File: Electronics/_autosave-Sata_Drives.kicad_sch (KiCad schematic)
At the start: 66 parts, among them J20 47018-2000, J21 47018-2000, Q2 NPN, Q3 PMOS, Q4 NPN, Q5 PMOS, Q6 PMOS, Q7 NPN, Q8 NPN, Q9 PMOS, U10 JMS561, U9 W25X40CLSN, Y1 30MHz

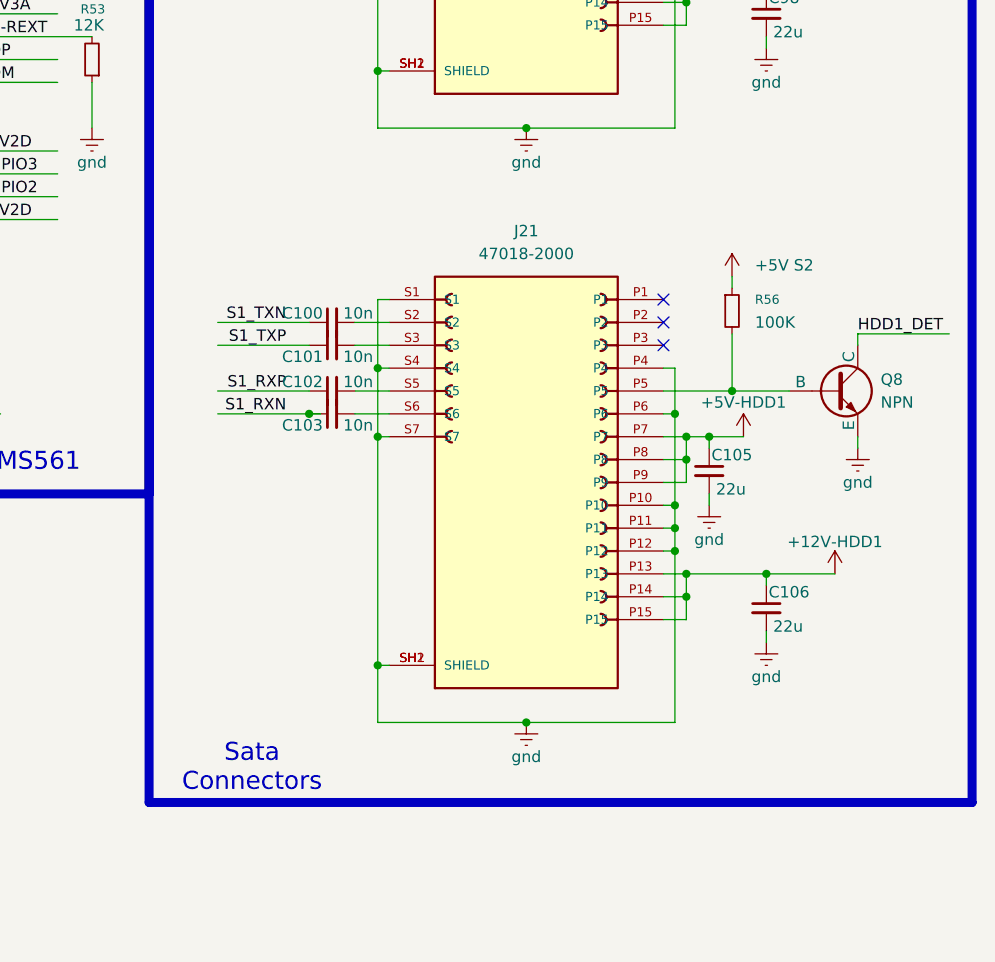
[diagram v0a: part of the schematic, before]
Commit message: Sata Port Changed
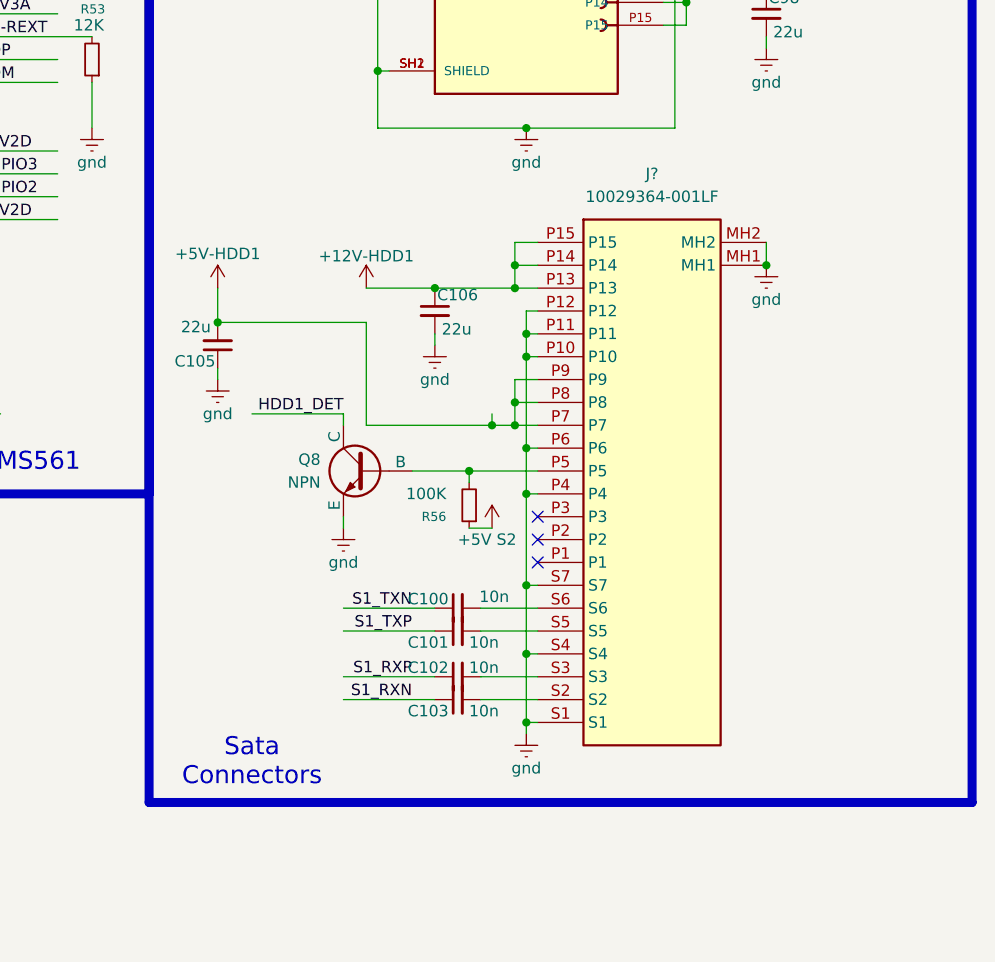
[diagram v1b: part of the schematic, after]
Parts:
- removed J21: 47018-2000, 47018-2000:MOLEX_47018-2000, symbol 47018-2000:47018-2000
- added J?: 10029364-001LF, 10029364001LF, symbol 10029364-001LF:10029364-001LF
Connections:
- net +12V-HDD1: now also J?.P13, J?.P14, J?.P15
- net +5V-HDD1: now also C105.2, J?.P7, J?.P8, J?.P9; no longer C105.1
- net gnd: now also C105.1, J?.MH1, J?.MH2, J?.P10, J?.P11, J?.P12, J?.P4, J?.P6, J?.S1, J?.S4, J?.S7; no longer C105.2
- net at C102.2: now also J?.S3
- net at C100.2: now also J?.S6
- net at Q8.2 (B), R56.2: now also J?.P5
- net at C101.2: now also J?.S5
- net at C103.2: now also J?.S2
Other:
- moved on the sheet: C100, C101, C102, C103, C105, C106, Q8, R56
